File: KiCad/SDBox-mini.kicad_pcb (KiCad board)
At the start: 2 copper layers, 36.7 x 23.1 mm, 2 parts, among them J1 DB25_Male

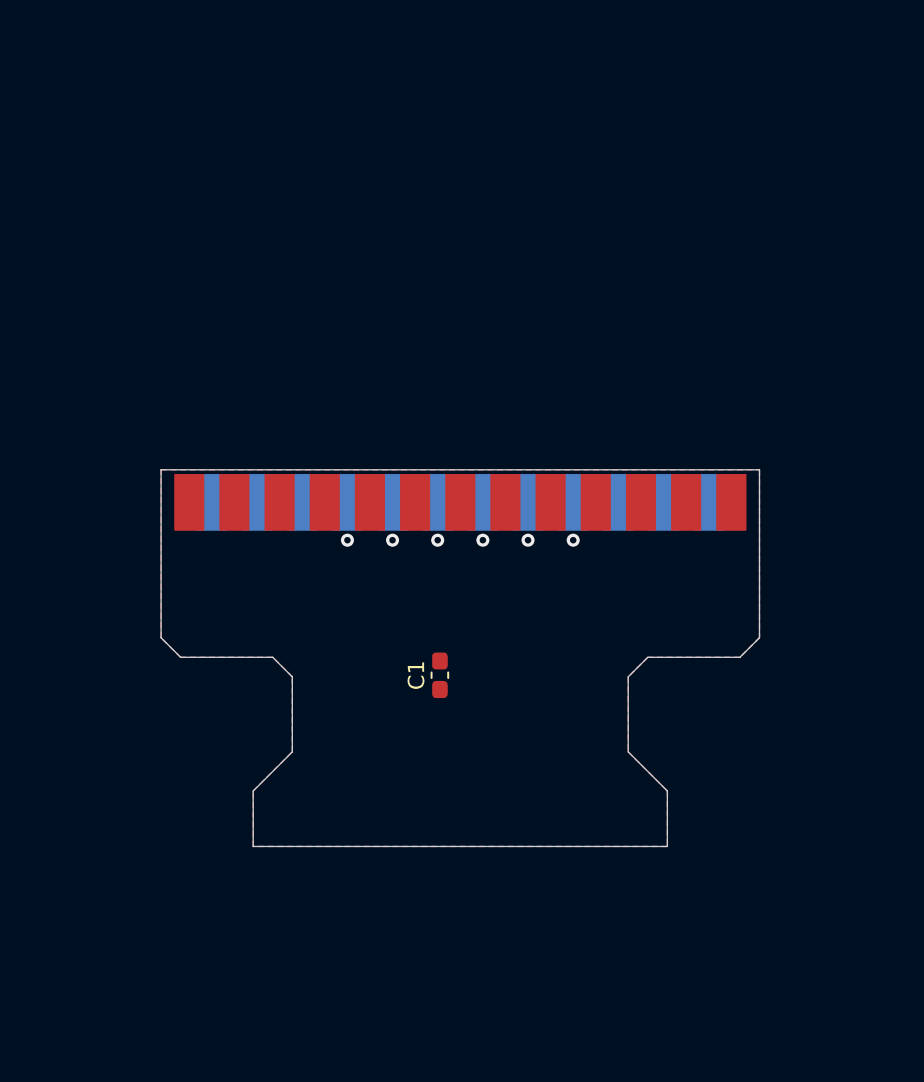
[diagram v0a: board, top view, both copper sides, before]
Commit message: resized PCB and added some components
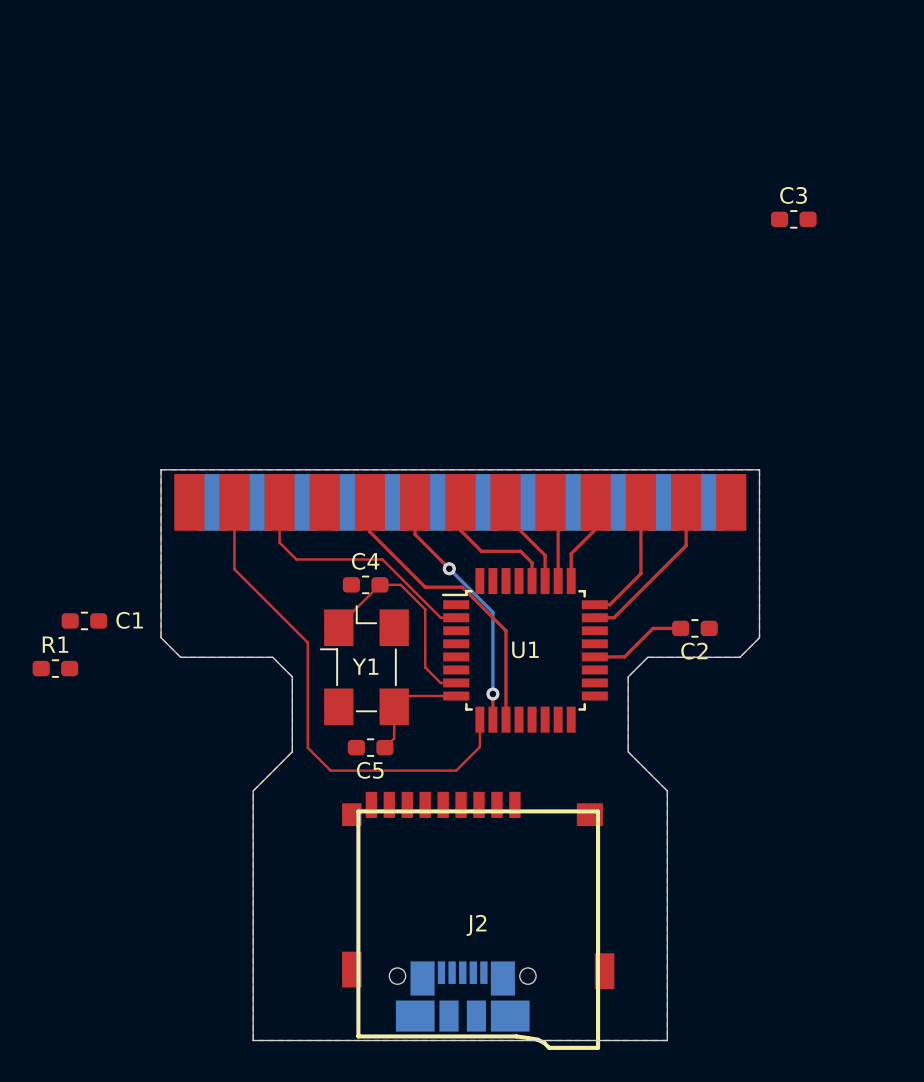
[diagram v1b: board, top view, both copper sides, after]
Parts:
- added C1: 0.1uF, Capacitor_SMD:C_0603_1608Metric_Pad1.05x0.95mm_HandSolder, F.Cu at (83.5, 59.3)
- added C3: 0.1uF, Capacitor_SMD:C_0603_1608Metric_Pad1.05x0.95mm_HandSolder, F.Cu at (127.0, 34.6)
- added C4: 16pF, Capacitor_SMD:C_0603_1608Metric_Pad1.05x0.95mm_HandSolder, F.Cu at (100.7, 57.1)
- added C5: 16pF, Capacitor_SMD:C_0603_1608Metric_Pad1.05x0.95mm_HandSolder, F.Cu at (101.0, 67.0)
- added J2: Micro_SD_Card, SDBox-mini:GCT-MEM2055-00-190-01-A, F.Cu at (107.6, 69.8)
- added R1: 10k, Resistor_SMD:R_0603_1608Metric_Pad1.05x0.95mm_HandSolder, F.Cu at (81.7, 62.2)
- added REF**: USB_Micro-B_Molex_47346-0001, Connector_USB:USB_Micro-B_Molex_47346-0001, B.Cu at (106.7, 82.3)
- added U1: ATmega328P-AU, Package_QFP:TQFP-32_7x7mm_P0.8mm, F.Cu at (110.5, 61.1)
- added Y1: Crystal_GND24_Small, Oscillator:Oscillator_SMD_Fordahl_DFAS15-4Pin_5.0x3.2mm_HandSoldering, F.Cu at (100.7, 62.1)
- moved C2 15.9 mm to (120.9, 59.7), turned to 180 degrees
- renumbered C1 to C2
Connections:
- net ACK renamed Net-(J1-Pad10)
- net STROBE renamed Net-(J1-Pad1)
- C2 pad 1: VCC -> GND
- C2 pad 2: GND -> /AREF
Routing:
- net POUT: track 0.00 -> 30.3 mm
- net D7: track 0.00 -> 18.1 mm
- net D6: track 0.00 -> 15.3 mm, vias 0 -> 2
- net BUSY: track 0.00 -> 15.2 mm
- net /XTAL1: track 0.00 -> 12.9 mm
- net D0: track 0.00 -> 10.1 mm
- net D5: track 0.00 -> 8.05 mm
- net D1: track 0.00 -> 7.99 mm
- net /XTAL2: track 0.00 -> 6.82 mm
- net /AREF: track 0.00 -> 5.99 mm
- net D4: track 0.00 -> 5.83 mm
- net D2: track 0.00 -> 5.45 mm
- net D3: track 0.00 -> 5.02 mm
- net GND: vias 6 -> 0
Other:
- board size 36.7 x 23.1 mm -> 36.7 x 35 mm

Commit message: added 3V3 voltage regulator, added 74LVC125A buffer
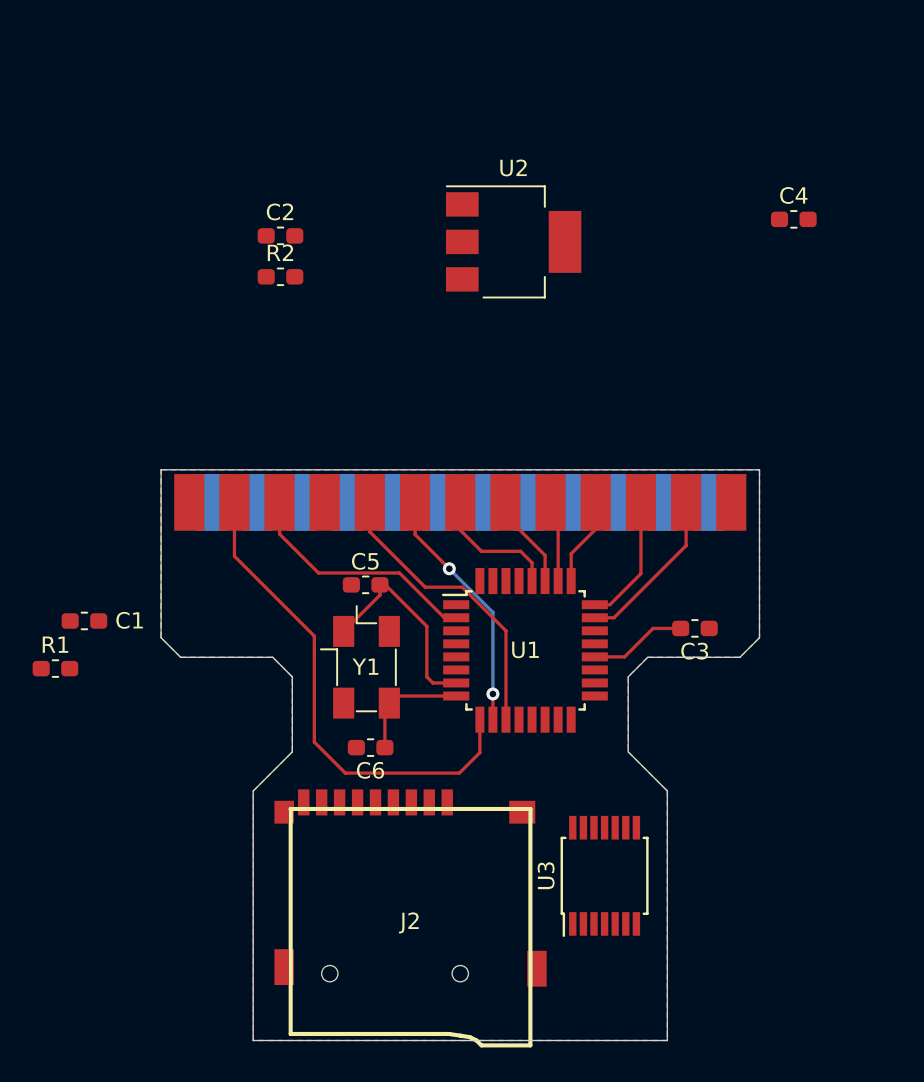
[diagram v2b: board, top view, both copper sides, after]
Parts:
- removed REF**: USB_Micro-B_Molex_47346-0001, Connector_USB:USB_Micro-B_Molex_47346-0001
- added C2: 0.1uF, Capacitor_SMD:C_0603_1608Metric_Pad1.05x0.95mm_HandSolder, F.Cu at (95.5, 35.7)
- added R2: 10k, Resistor_SMD:R_0603_1608Metric_Pad1.05x0.95mm_HandSolder, F.Cu at (95.5, 38.2)
- added U2: LM1117-3.3, Package_TO_SOT_SMD:SOT-223, F.Cu at (109.8, 36.0)
- added U3: 74LVC125A, Package_SO:TSSOP-14_4.4x5mm_P0.65mm, F.Cu at (115.3, 74.9)
- Y1: footprint Oscillator:Oscillator_SMD_Fordahl_DFAS15-4Pin_5.0x3.2mm_HandSoldering -> SDBox-mini:Crystal_EuroQuartz_SMD_4Pin_5.0x3.2mm
- moved J2 4.15 mm to (103.5, 69.6)
- renumbered C2 to C3, C3 to C4, C4 to C5, C5 to C6
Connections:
- J2 pad 2: CS -> SELECT_3V3
- J2 pad 3: MOSI -> MOSI_3V3
- J2 pad 5: SCK -> SCK_3V3
- J2 pad 7: MISO -> MISO_3V3

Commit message: added FTDI header
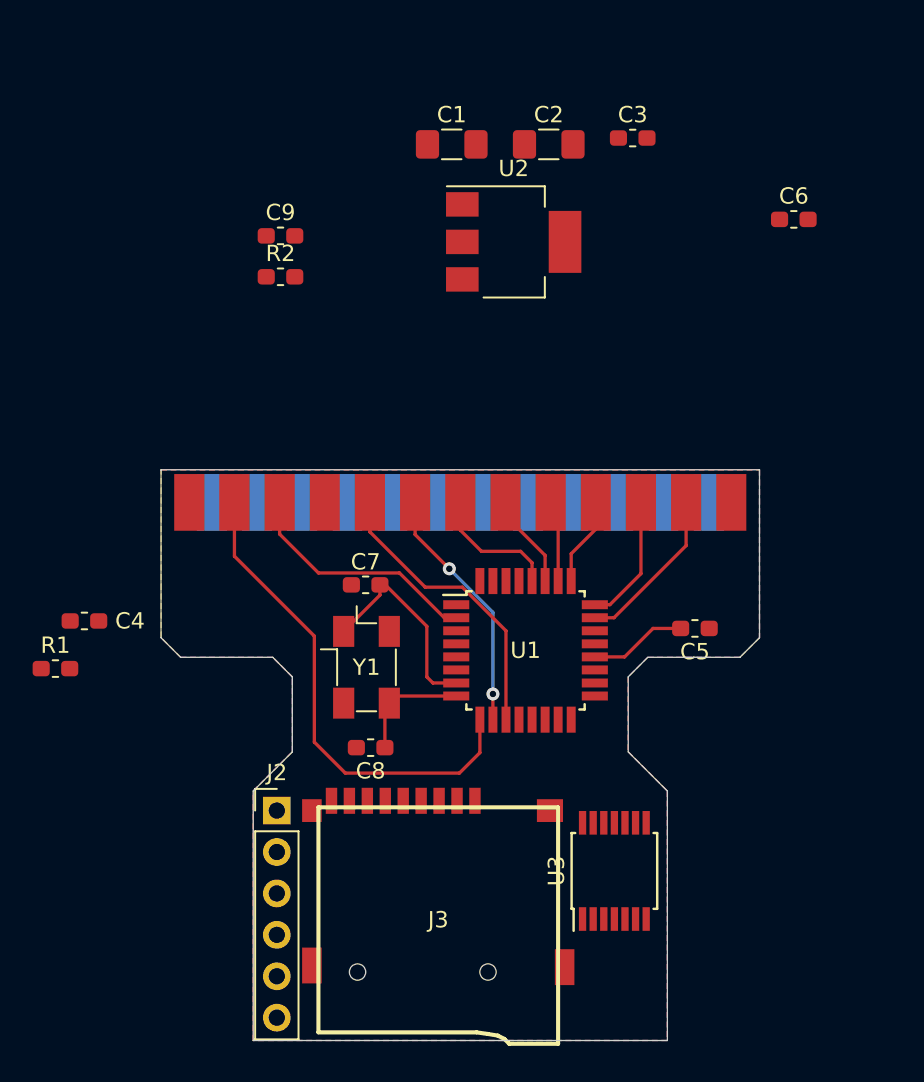
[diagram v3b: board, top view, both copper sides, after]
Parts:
- added C1: 10uF, Capacitor_SMD:C_1206_3216Metric_Pad1.42x1.75mm_HandSolder, F.Cu at (106.0, 30.0)
- added C2: 10uF, Capacitor_SMD:C_1206_3216Metric_Pad1.42x1.75mm_HandSolder, F.Cu at (111.9, 30.0)
- added C3: 0.1uF, Capacitor_SMD:C_0603_1608Metric_Pad1.05x0.95mm_HandSolder, F.Cu at (117.1, 29.7)
- added J2: Conn_01x06, Connector_PinHeader_2.54mm:PinHeader_1x06_P2.54mm_Vertical, F.Cu at (95.2, 70.9)
- moved J3 1.70 mm to (105.2, 69.5)
- moved U3 0.67 mm to (116.0, 74.6)
- renumbered C1 to C4, C3 to C5, C4 to C6, C5 to C7, C6 to C8, C2 to C9, J2 to J3
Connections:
- C9 pad 2: VCC -> 3V3
- U2 pad 1: Net-(U2-Pad1) -> GND
- U2 pad 2: Net-(U2-Pad2) -> 3V3
- U2 pad 3: Net-(U2-Pad3) -> VCC
- U2 pad 4: Net-(U2-Pad4) -> 3V3
- U3 pad 14: VCC -> 3V3

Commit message: changed to 74LVC3G17
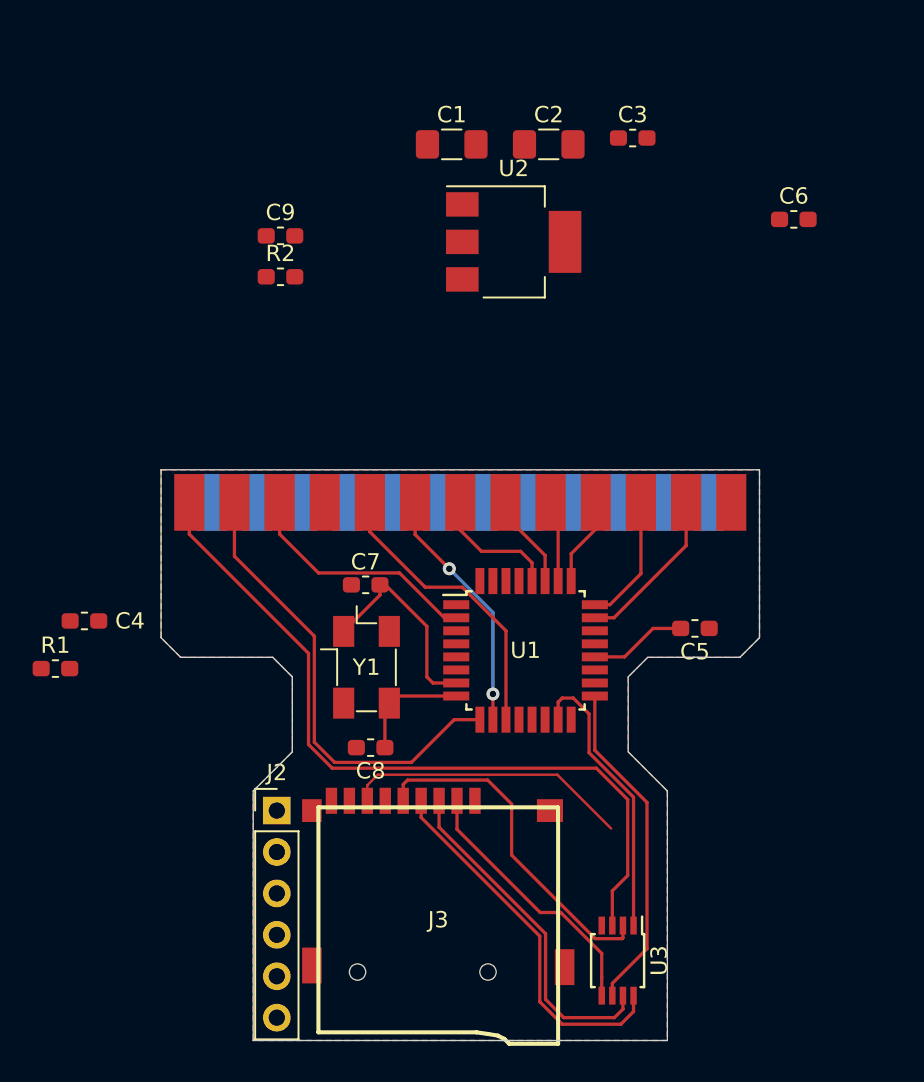
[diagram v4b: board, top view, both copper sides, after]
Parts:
- U3: value 74LVC125A -> 74LVC3G17; footprint Package_SO:TSSOP-14_4.4x5mm_P0.65mm -> Package_SO:TSSOP-8_3x3mm_P0.65mm
- moved U3 5.50 mm to (116.2, 80.1), turned to 270 degrees
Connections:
- C9 pad 1: GND -> 3V3
- C9 pad 2: 3V3 -> GND
- U3 pad 1: GND -> MOSI
- U3 pad 2: MOSI -> SCK_3V3
- U3 pad 3: MOSI_3V3 -> SELECT
- U3 pad 5: SCK -> SELECT_3V3
- U3 pad 6: SCK_3V3 -> SCK
- U3 pad 7: GND -> MOSI_3V3
- U3 pad 8: SELECT_3V3 -> 3V3
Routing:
- net SELECT: track 0.00 -> 48.0 mm
- net 3V3: track 0.00 -> 23.0 mm
- net SCK_3V3: track 0.00 -> 21.2 mm
- net MOSI_3V3: track 0.00 -> 21.1 mm
- net SCK: track 0.00 -> 20.6 mm
- net MISO_3V3: track 0.00 -> 18.2 mm
- net MOSI: track 0.00 -> 17.6 mm
- net SELECT_3V3: track 0.00 -> 16.4 mm
- net POUT: track 30.2 -> 28.5 mm

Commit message: added USB micro jack, and Dual non-inverting Schmitt trigger, and debounce circuit for card detect
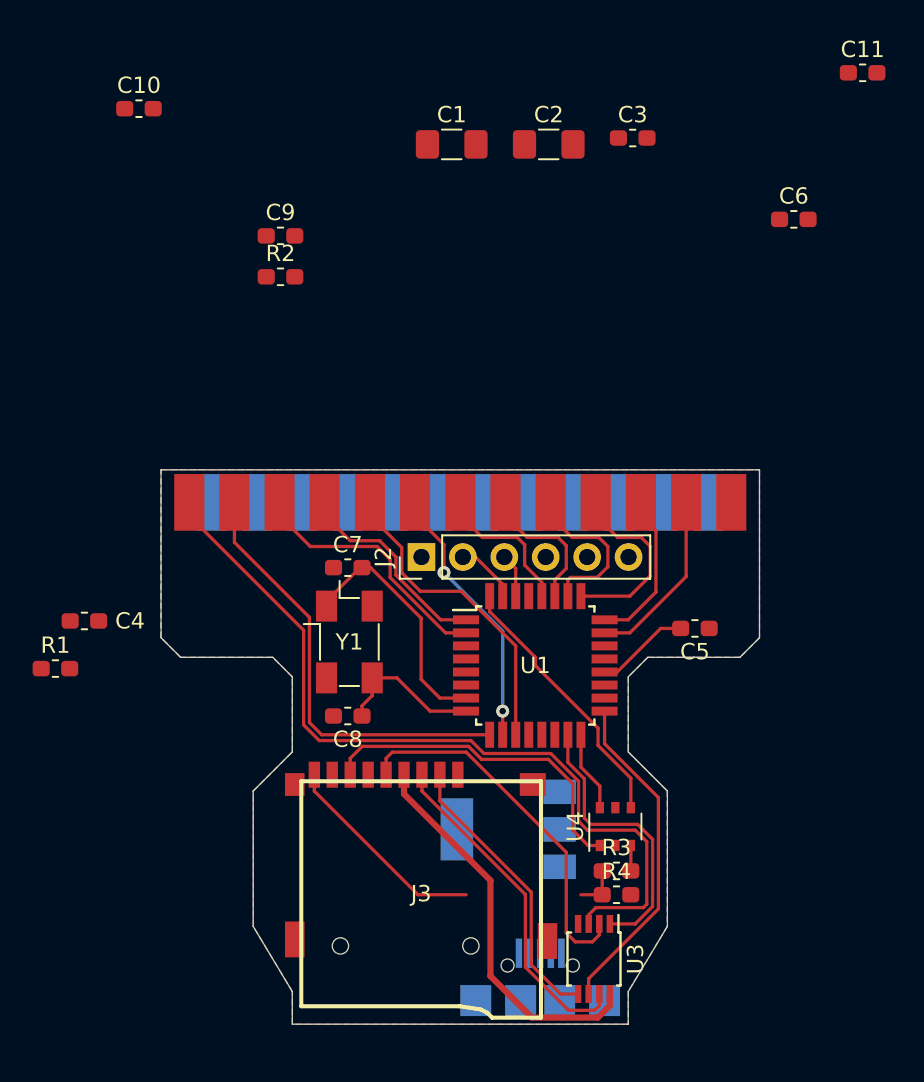
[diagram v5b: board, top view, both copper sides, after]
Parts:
- added C10: 0.1uF, Capacitor_SMD:C_0603_1608Metric_Pad1.05x0.95mm_HandSolder, F.Cu at (86.8, 27.9)
- added C11: 0.1uF, Capacitor_SMD:C_0603_1608Metric_Pad1.05x0.95mm_HandSolder, F.Cu at (131.2, 25.7)
- added J4: USB_B_Micro, SDBox-mini:USB_Micro-B_Unknown_5s_SMT, B.Cu at (111.4, 80.2)
- added R3: 10k, Resistor_SMD:R_0603_1608Metric_Pad1.05x0.95mm_HandSolder, F.Cu at (116.1, 74.6)
- added R4: 10k, Resistor_SMD:R_0603_1608Metric_Pad1.05x0.95mm_HandSolder, F.Cu at (116.1, 76.1)
- added U4: 74HCT2G17, Package_SO:TSOP-6_1.65x3.05mm_P0.95mm, F.Cu at (116.0, 71.9)
- U2: moved to B.Cu
- moved U2 36.0 mm to (109.4, 72.0), turned to 180 degrees
- moved J2 17.9 mm to (104.1, 55.4), turned to 90 degrees
- moved C8 2.39 mm to (99.6, 65.1)
- moved J3 1.91 mm to (104.1, 67.9)
- moved Y1 1.87 mm to (99.7, 60.6)
- moved C7 1.52 mm to (99.6, 56.0)
- moved U3 1.45 mm to (114.7, 80.0)
- moved U1 1.10 mm to (111.1, 62.0)
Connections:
- net SELECT_3V3 renamed CS
- C3 pad 1: 3V3 -> GND
- C3 pad 2: GND -> 3V3
- J1 pad 1: Net-(J1-Pad1) -> (no net)
- J1 pad 10: Net-(J1-Pad10) -> ACK
- J1 pad 14: Net-(J1-Pad14) -> (no net)
- J1 pad 15: Net-(J1-Pad15) -> (no net)
- J1 pad 23: Net-(J1-Pad23) -> (no net)
- J1 pad 24: Net-(J1-Pad24) -> (no net)
- J1 pad 25: Net-(J1-Pad25) -> (no net)
- J3 pad 1: Net-(J3-Pad1) -> (no net)
- J3 pad 10: (no net) -> GND
- J3 pad 8: Net-(J3-Pad8) -> (no net)
- J3 pad 9: Net-(J3-Pad9) -> CARD_DETECT
- U1 pad 1: Net-(U1-Pad1) -> ACK
- U1 pad 12: Net-(U1-Pad12) -> (no net)
- U1 pad 13: Net-(U1-Pad13) -> (no net)
- U1 pad 14: Net-(U1-Pad14) -> (no net)
- U1 pad 19: Net-(U1-Pad19) -> (no net)
- U1 pad 22: Net-(U1-Pad22) -> (no net)
- U1 pad 32: Net-(U1-Pad32) -> CD
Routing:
- net CD: track 0.00 -> 16.6 mm
- net CARD_DETECT: track 0.00 -> 15.7 mm
- net ACK: track 0.00 -> 12.8 mm
- net D2: track 5.45 -> 11.5 mm
- net D3: track 5.02 -> 10.2 mm
- net MISO: track 0.00 -> 4.95 mm
- net TXO: track 0.00 -> 3.86 mm
- net D4: track 5.83 -> 8.70 mm
- net RXI: track 0.00 -> 2.69 mm
- net MISO_3V3: track 18.2 -> 20.8 mm
- net /XTAL1: track 12.8 -> 15.2 mm
- net SELECT: track 48.0 -> 50.2 mm
- net /XTAL2: track 7.12 -> 9.19 mm
- net D6: track 15.3 -> 17.3 mm
- net D1: track 7.99 -> 9.74 mm
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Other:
- board size 36.7 x 35 mm -> 36.7 x 34 mm
